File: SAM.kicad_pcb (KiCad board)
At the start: 2 copper layers, 136.5 x 75.2 mm, 33 parts, among them J1 Bus_Apple_II_Card_Side, U1 DAC08, U2 L7805, U3 LM380N, U4 74LS273

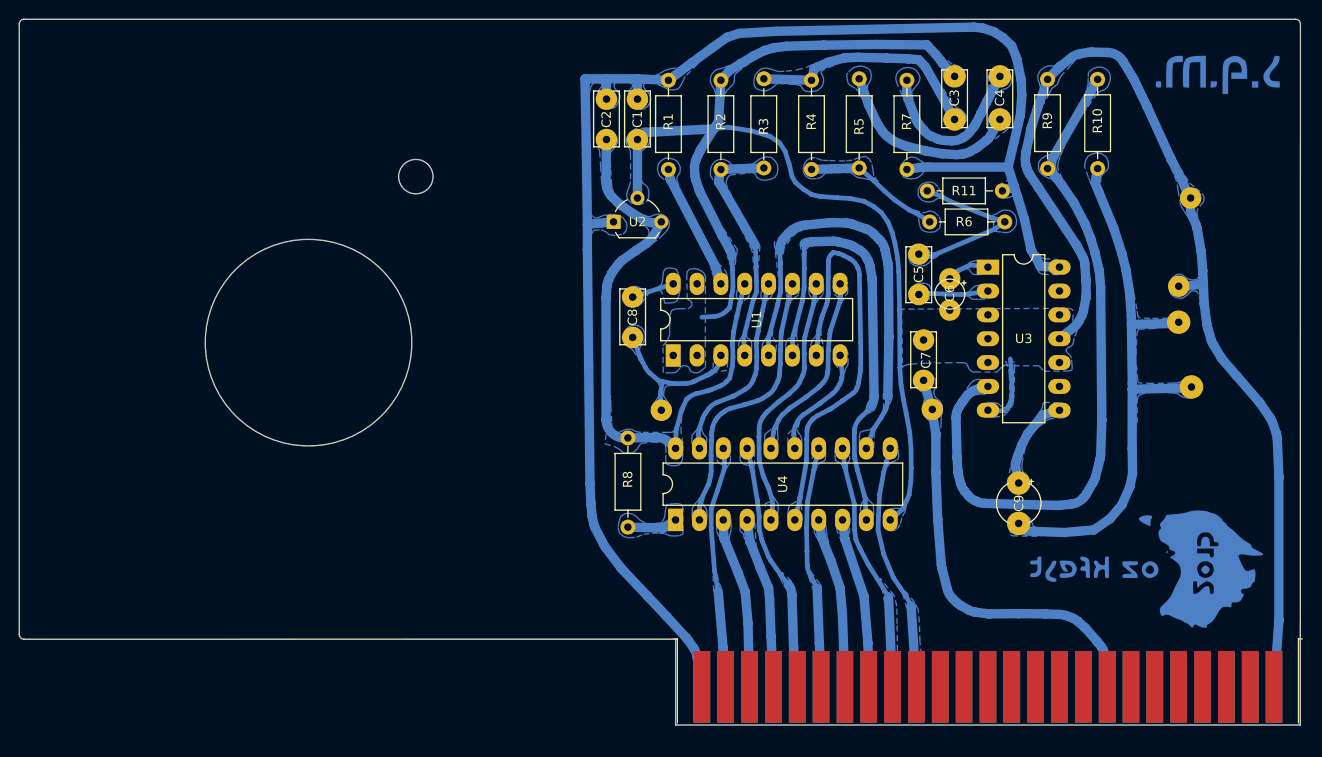
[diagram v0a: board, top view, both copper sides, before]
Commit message: Fix Apple II slot dimensions
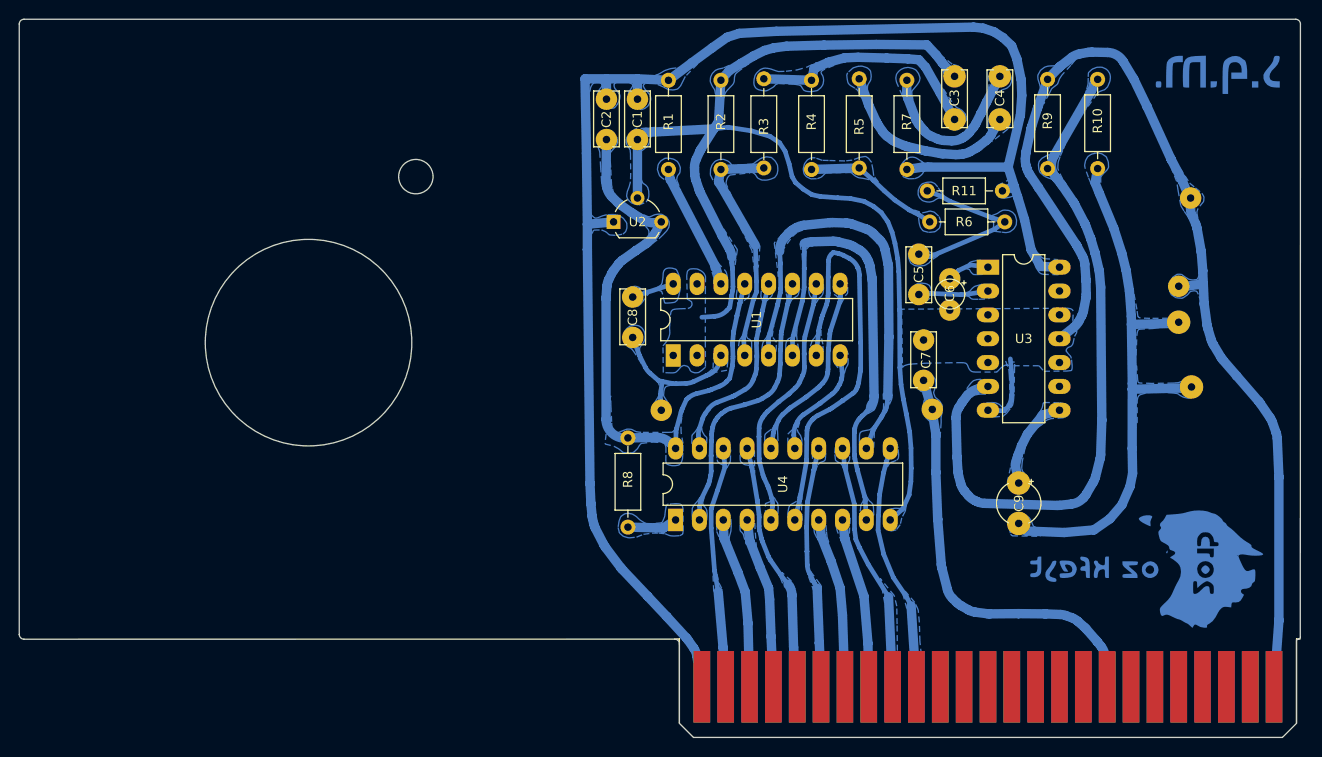
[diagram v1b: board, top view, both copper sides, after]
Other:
- board size 136.5 x 75.2 mm -> 136.5 x 76.5 mm

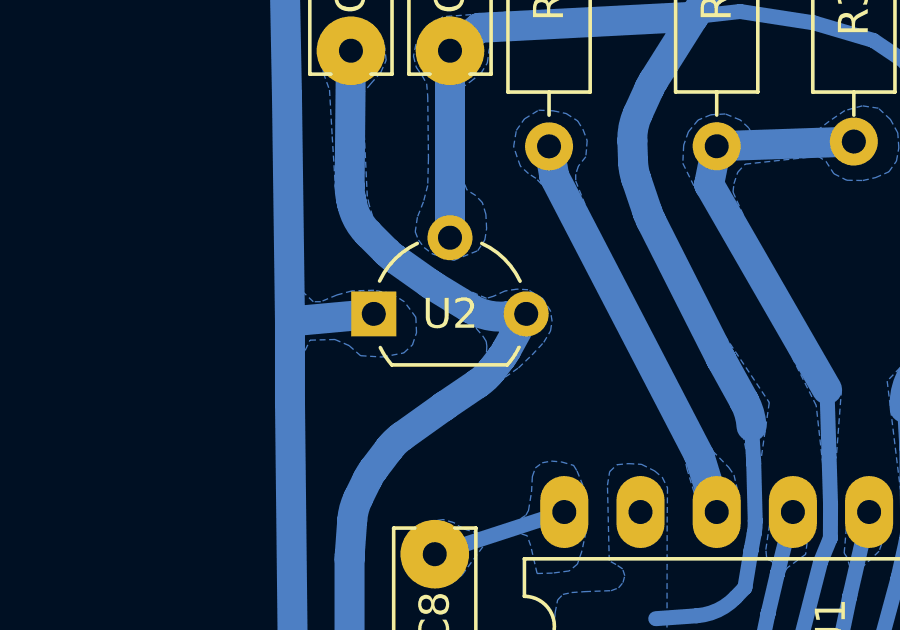
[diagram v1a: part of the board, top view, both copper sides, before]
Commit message: change 7805 to 78L05
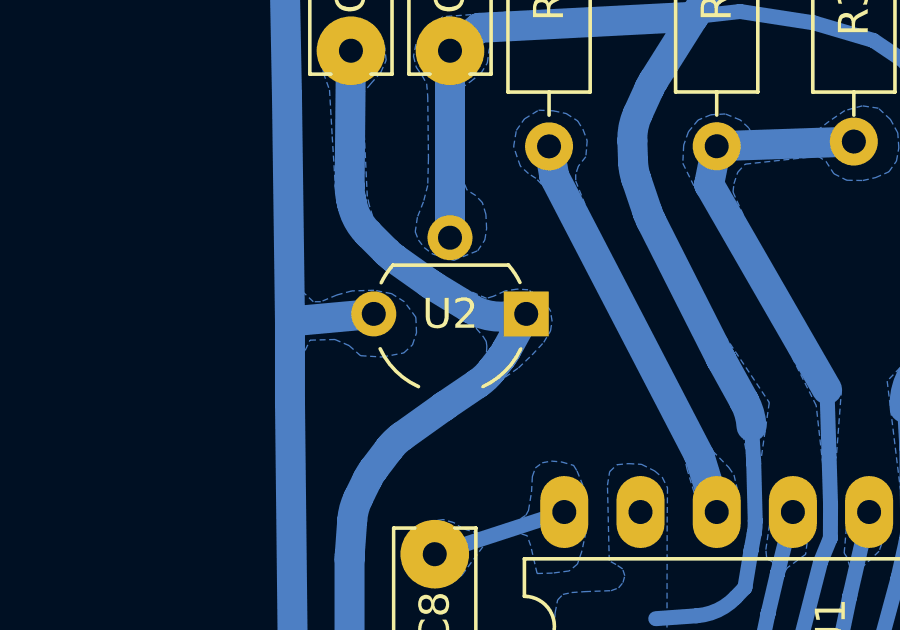
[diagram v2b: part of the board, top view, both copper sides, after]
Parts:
- U2: value L7805 -> L78L05
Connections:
- U2 pad 1: +12V -> +5V
- U2 pad 3: +5V -> +12V
